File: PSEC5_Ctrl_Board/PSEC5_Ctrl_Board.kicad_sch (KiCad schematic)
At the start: 1 part, among them U1 SM-K26-XCL2GI

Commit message: Beginning Build of Ctrlbd Schematic
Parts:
- removed U1: SM-K26-XCL2GI, SM-K26-XCL2GI:MODULE_SM-K26-XCL2GI, symbol kriak26:SM-K26-XCL2GI
- added J3, J4: ADM6-60-01.5-L-4-2-A-TR, ADM6-60-01.5-L-4-2-A-TR:SAMTEC_ADM6-60-01.5-L-4-2-A-TR, symbol PSEC5_ctrlbd:ADM6-60-01.5-L-4-2-A-TR
- added J5: QSH-040-01-X-D-DP-A, QSH-040-01-X-D-DP-A:SAMTEC_QSH-040-01-X-D-DP-A, symbol PSEC5_ctrlbd:QSH-040-01-X-D-DP-A
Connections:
- new net A01: J3.A01, J4.A01
- new net A02: J3.A02, J4.A02
- new net A05: J3.A05, J4.A05
- new net A06: J3.A06, J4.A06
- new net A09: J3.A09, J4.A09
- new net A10: J3.A10, J4.A10
- new net A13: J3.A13, J4.A13
- new net A16: J3.A16, J4.A16
- new net A19: J3.A19, J4.A19
- new net A22: J3.A22, J4.A22
- new net A25: J3.A25, J4.A25
- new net A28: J3.A28, J4.A28
- new net A31: J3.A31, J4.A31
- new net A34: J3.A34, J4.A34
- new net A37: J3.A37, J4.A37
- new net A40: J3.A40, J4.A40
- new net A43: J3.A43, J4.A43
- new net A45: J3.A45, J4.A45
- new net A49: J3.A49, J4.A49
- new net A53: J3.A53, J4.A53
- new net A57: J3.A57, J4.A57
- new net B03: J3.B03, J4.B03
- new net B04: J3.B04, J4.B04
- new net B07: J3.B07, J4.B07
- new net B08: J3.B08, J4.B08
- new net B11: J3.B11, J4.B11
- new net B14: J3.B14, J4.B14
- new net B17: J3.B17, J4.B17
- new net B20: J3.B20, J4.B20
- new net B23: J3.B23, J4.B23
- new net B26: J3.B26, J4.B26
- new net B29: J3.B29, J4.B29
- new net B32: J3.B32, J4.B32
- new net B35: J3.B35, J4.B35
- new net B38: J3.B38, J4.B38
- new net B41: J3.B41, J4.B41
- new net B43: J3.B43, J4.B43
- new net B47: J3.B47, J4.B47
- new net B51: J3.B51, J4.B51
- new net B55: J3.B55, J4.B55
- new net CLKOUT: J3.A38, J5.23
- new net DISCBIAS: J4.B39, J5.24
- new net GND: J5.G1 (GND_S1), J5.G2 (GND_S1__1), J5.G3 (GND_S1__2), J5.G4 (GND_S1__3)
- new net HBD_power: J3.B59, J3.B60, J4.B59, J4.B60
- new net PICO: J4.B16, J5.33
- new net POCI: J3.A12, J5.03
- new net READBIAS1: J4.B34, J5.18
- new net READBIAS2: J4.B36, J5.20
- new net READCLK: J4.B12, J5.27
- new net READOUT1: J3.A14, J5.05
- new net READOUT2: J3.A15, J5.07
- new net READOUT3: J3.A17, J5.09
- new net READOUT4: J3.A18, J5.11
- new net READOUT5: J3.A20, J5.13
- new net READOUT6: J3.A21, J5.15
- new net READOUT7: J3.A23, J5.17
- new net READOUT8: J3.A24, J5.19
- new net REFCLKOUT: J3.A39, J5.25
- new net RESET: J4.B18, J5.35
- new net SIGNAL1: J4.B40, J5.26
- new net SIGNAL2: J4.B44, J5.28
- new net SIGNAL3: J4.B45, J5.30
- new net SIGNAL4: J4.B46, J5.32
- new net SIGNAL5: J4.B48, J5.34
- new net SIGNAL6: J4.B49, J5.36
- new net SIGNAL7: J5.38
- new net SIGNAL8: J4.B52, J5.40
- new net SIGNAl7: J4.B50
- new net SPICLK: J4.B19, J5.37
- new net THRES1: J4.B22, J5.02
- new net THRES2: J4.B24, J5.04
- new net THRES3: J4.B25, J5.06
- new net THRES4: J4.B27, J5.08
- new net THRES5: J4.B28, J5.10
- new net THRES6: J4.B30, J5.12
- new net THRES7: J4.B31, J5.14
- new net THRES8: J4.B33, J5.16
- new net TRIGGERIN: J4.B13, J5.29
- new net TRIGGEROUT: J3.A26, J5.21
- new net VCOCTRL: J4.B15, J5.31
- new net WBUFBIAS: J4.B37, J5.22
- new net postp_VTUNE: J4.B21, J5.39
- new net prep_VTUNE: J3.A11, J5.01
- new net pwr_1.0_1.8: J3.A44, J3.B42, J4.A44, J4.B42
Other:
- added sheet JTAG (JTAG.kicad_sch)
- note added: "INPUTS"
- note added: "OUTPUTS"

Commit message: A lil more to ctlrbrd, more to come very soon
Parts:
- added J9: QSH-040-01-X-D-DP-A, QSH-040-01-X-D-DP-A:SAMTEC_QSH-040-01-X-D-DP-A, symbol PSEC5_ctrlbd:QSH-040-01-X-D-DP-A
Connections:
- net CLKOUT: no longer J5.23
- net DISCBIAS: now also J5.39; no longer J4.B39, J5.24
- net GND: now also J9.G1 (GND_S1), J9.G2 (GND_S1__1), J9.G3 (GND_S1__2), J9.G4 (GND_S1__3)
- net PICO: now also J9.11; no longer J4.B16, J5.33
- net POCI: now also J9.09; no longer J5.03
- net READBIAS1: now also J5.33; no longer J4.B34, J5.18
- net READBIAS2: now also J5.35; no longer J4.B36, J5.20
- net READOUT1: no longer J5.05
- net READOUT2: no longer J5.07
- net READOUT3: no longer J5.09
- net READOUT4: no longer J5.11
- net READOUT5: no longer J5.13
- net READOUT6: no longer J5.15
- net READOUT7: no longer J5.17
- net READOUT8: no longer J5.19
- net REFCLKOUT: no longer J5.25
- net THRES1: now also J5.01; no longer J4.B22, J5.02
- net THRES2: now also J5.03; no longer J4.B24, J5.04
- net THRES3: now also J5.05; no longer J4.B25, J5.06
- net THRES4: now also J5.07; no longer J4.B27, J5.08
- net THRES5: now also J5.09; no longer J4.B28, J5.10
- net THRES6: now also J5.11; no longer J4.B30, J5.12
- net THRES7: now also J5.13; no longer J4.B31, J5.14
- net THRES8: now also J5.15; no longer J4.B33, J5.16
- net TRIGGEROUT: no longer J5.21
- net WBUFBIAS: now also J5.37; no longer J4.B37, J5.22
- net prep_VTUNE: no longer J5.01
- net READCLK: no longer names the net of J4.B12
- net READCLK: no longer J5.27
- net RESET: no longer names the net of J4.B18
- net RESET: no longer J5.35
- net SIGNAL1: no longer names the net of J4.B40
- net SIGNAL1: no longer J5.26
- net SIGNAL2: no longer names the net of J4.B44
- net SIGNAL2: no longer J5.28
- net SIGNAL3: no longer names the net of J4.B45
- net SIGNAL3: no longer J5.30
- net SIGNAL4: no longer names the net of J4.B46
- net SIGNAL4: no longer J5.32
- net SIGNAL5: no longer names the net of J4.B48
- net SIGNAL5: no longer J5.34
- net SIGNAL6: no longer names the net of J4.B49
- net SIGNAL6: no longer J5.36
- net SIGNAL7 renamed SIGNAL8+
- net SIGNAL8: no longer names the net of J4.B52
- net SIGNAL8: no longer J5.40
- net SIGNAl7: no longer names the net of J4.B50
- net SPICLK: no longer names the net of J4.B19
- net SPICLK: no longer J5.37
- net TRIGGERIN: no longer names the net of J4.B13
- net TRIGGERIN: no longer J5.29
- net VCOCTRL: no longer names the net of J4.B15
- net VCOCTRL: no longer J5.31
- net postp_VTUNE: no longer names the net of J4.B21
- net postp_VTUNE: no longer J5.39
- new net 1V2: J9.02
- new net 1V8: J9.04
- new net 2V5: J9.06
- new net 3V3: J9.08
- new net 5V: J9.10
- new net ADC_SCLK: J9.29
- new net ADC_SDO: J9.33
- new net DAC_SCLK: J9.21
- new net DAC_V_IN: J9.27
- new net OscRefClk: J9.01
- new net Psec5RST: J9.15
- new net Psec5ReadClk: J9.17
- new net Psec5RefClk: J9.03
- new net Psec5TriggerIn: J9.07
- new net Psec5TriggerOut: J9.05
- new net SIGNAL1+: J5.02
- new net SIGNAL1-: J5.04
- new net SIGNAL2+: J5.06
- new net SIGNAL2-: J5.08
- new net SIGNAL3+: J5.10
- new net SIGNAL3-: J5.12
- new net SIGNAL4+: J5.14
- new net SIGNAL4-: J5.16
- new net SIGNAL5+: J5.26
- new net SIGNAL5-: J5.28
- new net SIGNAL6+: J5.30
- new net SIGNAL6-: J5.32
- new net SIGNAL7+: J5.34
- new net SIGNAL7-: J5.36
- new net SIGNAL8-: J5.40
- new net SPIClk: J9.13
- new net SYNC_N: J9.25
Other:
- added sheet SDcard (SDcard.kicad_sch)
- added sheet USB-UART (USBUART.kicad_sch)
- added sheet adcdac (adccad.kicad_sch)
- added sheet ethernet (ethernet.kicad_sch)
- added sheet samtectest (samtectest.kicad_sch)
- sheet Peripherals_Ctrl ports: added ADC_1.8AVDD, ADC_1.8DVDD, ADC_CLK+, ADC_CLK-, ADC_DOUT1+, ADC_DOUT1-, ADC_DOUT2+, ADC_DOUT2-, ADC_DOUT3+, ADC_DOUT3-, ADC_DOUT4+, ADC_DOUT4-, ADC_DOUT5+, ADC_DOUT5-, ADC_DOUT6+, ADC_DOUT6-, ADC_DOUT7+, ADC_DOUT7-, ADC_DOUT8+, ADC_DOUT8-, ADC_VREF, DCO+, DCO-, FCO+, FCO-, READOUT1+, READOUT1-, READOUT2+, READOUT2-, READOUT3+, READOUT3-, READOUT4+, READOUT4-, READOUT5+, READOUT5-, READOUT6+, READOUT6-, READOUT7+, READOUT7-, READOUT8+, READOUT8-; removed none
- note added: "ANALOG SAMTEC"
- note added: "DIGITAL SAMTEC + OTHER"
- note removed: "INPUTS"
- note removed: "OUTPUTS"
- moved on the sheet: J3A, J4A

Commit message: Ports are Finished, wiring and finalization needed
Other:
- sheet JTAG ports: added CLK, RST, TDI, TDO, TMS; removed none
- sheet USB-UART ports: added CTS, RTS, RXD, TXD; removed none
- sheet ethernet ports: added 25MHz, ETH_MDC, ETH_MDIO, ETH_RXD0, ETH_RXD1, ETH_RXD2, ETH_RXD3, ETH_RX_CLK, ETH_RX_CTRL, ETH_TXD0, ETH_TXD1, ETH_TXD2, ETH_TXD3, ETH_TX_CLK, ETH_TX_CTRL, RESETn; removed none

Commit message: Large Updates, Touching up before further aproval
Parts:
- removed J3, J4: ADM6-60-01.5-L-4-2-A-TR, ADM6-60-01.5-L-4-2-A-TR:SAMTEC_ADM6-60-01.5-L-4-2-A-TR, symbol PSEC5_ctrlbd:ADM6-60-01.5-L-4-2-A-TR
- removed J5, J9: QSH-040-01-X-D-DP-A, QSH-040-01-X-D-DP-A:SAMTEC_QSH-040-01-X-D-DP-A, symbol PSEC5_ctrlbd:QSH-040-01-X-D-DP-A
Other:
- removed sheet IO
- removed sheet samtectest
- added sheet DUT_CTRL (DUT_CTRL.kicad_sch)
- added sheet SOM240_1(1.5) (untitled.SOM240_1(1.5).kicad_sch)
- added sheet SOM240_2(1.5) (untitled.SOM240_2(1.5).kicad_sch)
- added sheet power (power.kicad_sch)
- note removed: "ANALOG SAMTEC"
- note removed: "DIGITAL SAMTEC + OTHER"

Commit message: Schematic is "done" ;( (999+ ERC errors)
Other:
- added sheet power2 (power2.kicad_sch)
- sheet JTAG ports: added none; removed CLK, RST, TDI, TDO, TMS
- sheet Peripherals_Ctrl ports: added none; removed ADC_1.8AVDD, ADC_1.8DVDD, ADC_CLK+, ADC_CLK-, ADC_DOUT1+, ADC_DOUT1-, ADC_DOUT2+, ADC_DOUT2-, ADC_DOUT3+, ADC_DOUT3-, ADC_DOUT4+, ADC_DOUT4-, ADC_DOUT5+, ADC_DOUT5-, ADC_DOUT6+, ADC_DOUT6-, ADC_DOUT7+, ADC_DOUT7-, ADC_DOUT8+, ADC_DOUT8-, ADC_VREF, DCO+, DCO-, FCO+, FCO-, READOUT1+, READOUT1-, READOUT2+, READOUT2-, READOUT3+, READOUT3-, READOUT4+, READOUT4-, READOUT5+, READOUT5-, READOUT6+, READOUT6-, READOUT7+, READOUT7-, READOUT8+, READOUT8-
- sheet SDcard ports: added none; removed SD_CLK, SD_CMD, SD_DAT0, SD_DAT1, SD_DAT2, SD_DAT3, SD_DETECT, SD_PWR_EN, SD_SEL
- sheet USB-UART ports: added none; removed CTS, RTS, RXD, TXD
- sheet ethernet ports: added none; removed 25MHz, ETH_MDC, ETH_MDIO, ETH_RXD0, ETH_RXD1, ETH_RXD2, ETH_RXD3, ETH_RX_CLK, ETH_RX_CTRL, ETH_TXD0, ETH_TXD1, ETH_TXD2, ETH_TXD3, ETH_TX_CLK, ETH_TX_CTRL, RESETn

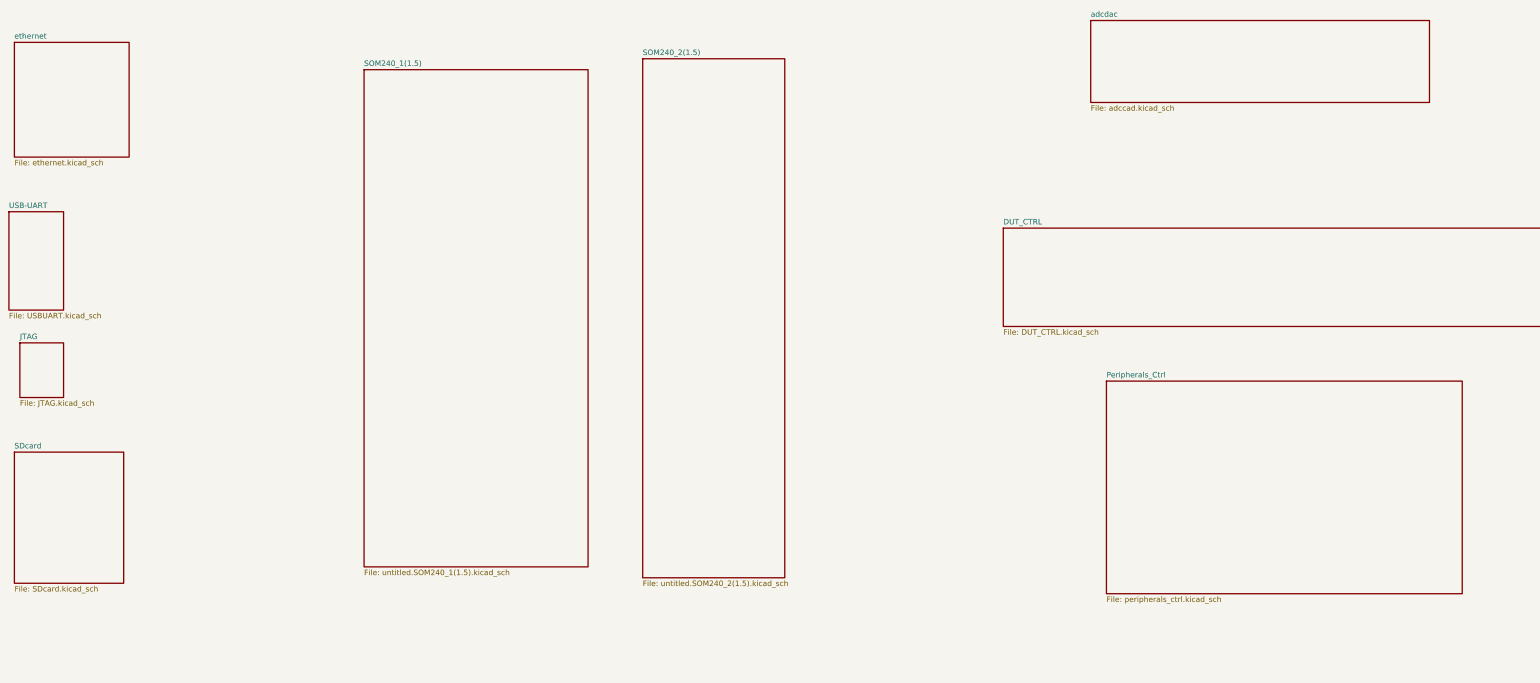
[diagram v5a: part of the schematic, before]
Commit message: Deleted some Pages, still lots of errors :(
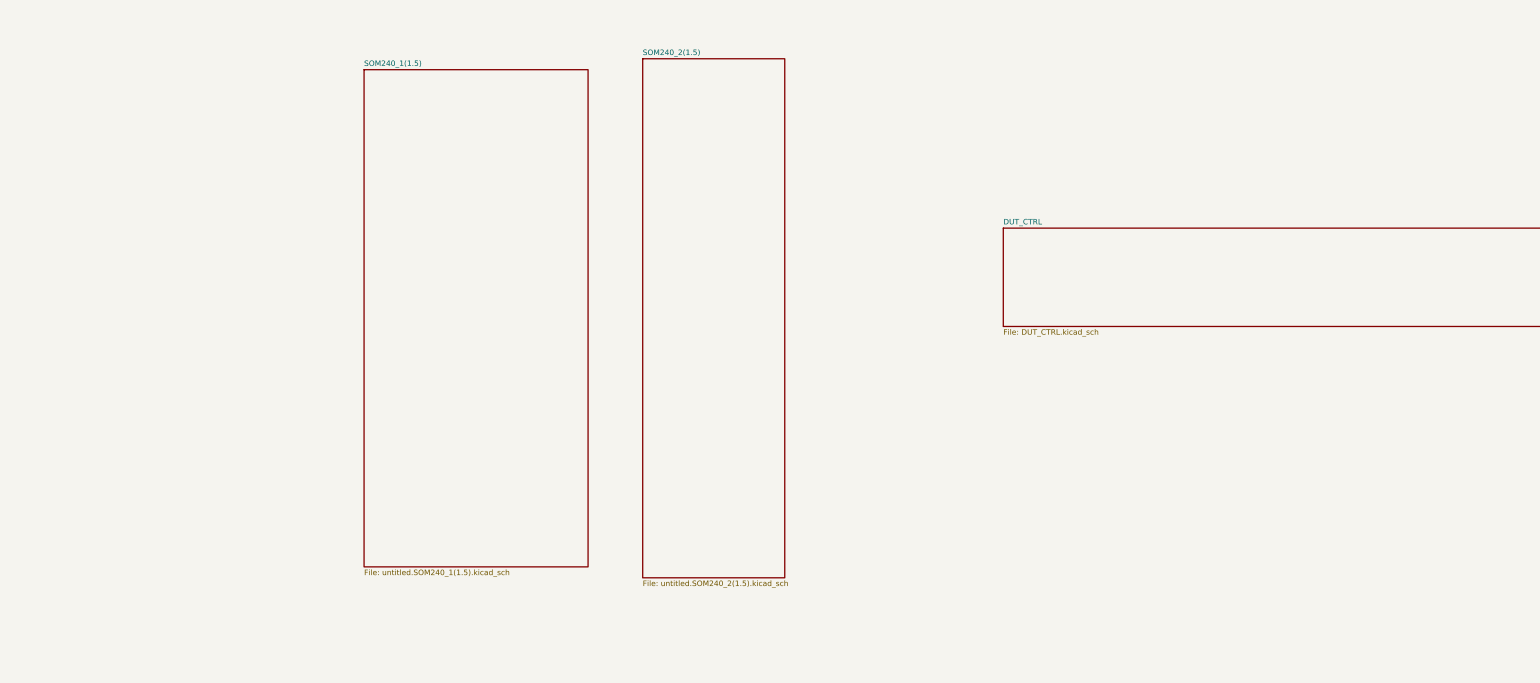
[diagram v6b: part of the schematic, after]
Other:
- removed sheet JTAG
- removed sheet Peripherals_Ctrl
- removed sheet SDcard
- removed sheet USB-UART
- removed sheet adcdac
- removed sheet ethernet
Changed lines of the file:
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@@
-	)
-	(sheet
-		(at 270.35 140.97)
-		(size 82.71 49.42)
-		(fields_autoplaced yes)
-		(stroke
-			(width 0.1524)
-			(type solid)
-		)
-		(fill
-			(color 0 0 0 0.0000)
-		)
-		(property "Sheetname" "Peripherals_Ctrl"
-			(at 270.35 140.2584 0)
-			(effects
-				(font
-					(size 1.27 1.27)
-				)
-				(justify left bottom)
-			)
-		)
-		(property "Sheetfile" "peripherals_ctrl.kicad_sch"
-			(at 270.35 190.9746 0)
-			(effects
-				(font
-					(size 1.27 1.27)
-				)
-				(justify left top)
-			)
-		)
-		(instances
-			(project "PSEC5_Ctrl_Board"
-				(path "/165f2ae6-d522-4adf-a6c4-bb137b209d33"
-					(page "5")
-				)
-			)
-		)
 	)
 	(sheet
@@
 	)
 	(sheet
-		(at 266.7 57.15)
-		(size 78.74 19.05)
-		(fields_autoplaced yes)
-		(stroke
-			(width 0.1524)
-			(type solid)
-		)
-		(fill
-			(color 0 0 0 0.0000)
-		)
-		(property "Sheetname" "adcdac"
-			(at 266.7 56.4384 0)
-			(effects
-				(font
-					(size 1.27 1.27)
-				)
-				(justify left bottom)
-			)
-		)
-		(property "Sheetfile" "adccad.kicad_sch"
-			(at 266.7 76.7846 0)
-			(effects
-				(font
-					(size 1.27 1.27)
-				)
-				(justify left top)
-			)
-		)
-		(instances
-			(project "PSEC5_Ctrl_Board"
-				(path "/165f2ae6-d522-4adf-a6c4-bb137b209d33"
-					(page "6")
-				)
-			)
-		)
-	)
-	(sheet
-		(at 16.51 62.23)
-		(size 26.67 26.67)
-		(fields_autoplaced yes)
-		(stroke
-			(width 0.1524)
-			(type solid)
-		)
-		(fill
-			(color 0 0 0 0.0000)
-		)
-		(property "Sheetname" "ethernet"
-			(at 16.51 61.5184 0)
-			(effects
-				(font
-					(size 1.27 1.27)
-				)
-				(justify left bottom)
-			)
-		)
-		(property "Sheetfile" "ethernet.kicad_sch"
-			(at 16.51 89.4846 0)
-			(effects
-				(font
-					(size 1.27 1.27)
-				)
-				(justify left top)
-			)
-		)
-		(instances
-			(project "PSEC5_Ctrl_Board"
-				(path "/165f2ae6-d522-4adf-a6c4-bb137b209d33"
-					(page "11")
-				)
-			)
-		)
-	)
-	(sheet
-		(at 16.51 157.48)
-		(size 25.4 30.48)
-		(fields_autoplaced yes)
-		(stroke
-			(width 0.1524)
-			(type solid)
-		)
-		(fill
-			(color 0 0 0 0.0000)
-		)
-		(property "Sheetname" "SDcard"
-			(at 16.51 156.7684 0)
-			(effects
-				(font
-					(size 1.27 1.27)
-				)
-				(justify left bottom)
-			)
-		)
-		(property "Sheetfile" "SDcard.kicad_sch"
-			(at 16.51 188.5446 0)
-			(effects
-				(font
-					(size 1.27 1.27)
-				)
-				(justify left top)
-			)
-		)
-		(instances
-			(project "PSEC5_Ctrl_Board"
-				(path "/165f2ae6-d522-4adf-a6c4-bb137b209d33"
-					(page "10")
-				)
-			)
-		)
-	)
-	(sheet
 		(at 49.53 227.33)
 		(size 109.22 43.18)
@@
 				)
 			)
-		)
-	)
-	(sheet
-		(at 15.24 101.6)
-		(size 12.7 22.86)
-		(fields_autoplaced yes)
-		(stroke
-			(width 0.1524)
-			(type solid)
-		)
-		(fill
-			(color 0 0 0 0.0000)
-		)
-		(property "Sheetname" "USB-UART"
-			(at 15.24 100.8884 0)
-			(effects
-				(font
-					(size 1.27 1.27)
-				)
-				(justify left bottom)
-			)
-		)
-		(property "Sheetfile" "USBUART.kicad_sch"
-			(at 15.24 125.0446 0)
-			(effects
-				(font
-					(size 1.27 1.27)
-				)
-				(justify left top)
-			)
-		)
-		(instances
-			(project "PSEC5_Ctrl_Board"
-				(path "/165f2ae6-d522-4adf-a6c4-bb137b209d33"
-					(page "9")
-				)
-			)
-		)
-	)
-	(sheet
-		(at 17.78 132.08)
-		(size 10.16 12.7)
-		(fields_autoplaced yes)
-		(stroke
-			(width 0.1524)
-			(type solid)
-		)
-		(fill
-			(color 0 0 0 0.0000)
-		)
-		(property "Sheetname" "JTAG"
-			(at 17.78 131.3684 0)
-			(effects
-				(font
-					(size 1.27 1.27)
-				)
-				(justify left bottom)
-			)
-		)
-		(property "Sheetfile" "JTAG.kicad_sch"
-			(at 17.78 145.3646 0)
-			(effects
-				(font
-					(size 1.27 1.27)
-				)
-				(justify left top)
-			)
-		)
-		(instances
-			(project "PSEC5_Ctrl_Board"
-				(path "/165f2ae6-d522-4adf-a6c4-bb137b209d33"
-					(page "8")
-				)
-			)

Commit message: ERC "Done" (4 errors left) Schematic "Done"
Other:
- added sheet power_ctrl (power_ctrl.kicad_sch)
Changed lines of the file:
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@@
+	)
+	(sheet
+		(at 35.56 86.36)
+		(size 25.4 50.8)
+		(fields_autoplaced yes)
+		(stroke
+			(width 0.1524)
+			(type solid)
+		)
+		(fill
+			(color 0 0 0 0.0000)
+		)
+		(property "Sheetname" "power_ctrl"
+			(at 35.56 85.6484 0)
+			(effects
+				(font
+					(size 1.27 1.27)
+				)
+				(justify left bottom)
+			)
+		)
+		(property "Sheetfile" "power_ctrl.kicad_sch"
+			(at 35.56 137.7446 0)
+			(effects
+				(font
+					(size 1.27 1.27)
+				)
+				(justify left top)
+			)
+		)
+		(instances
+			(project "PSEC5_Ctrl_Board"
+				(path "/165f2ae6-d522-4adf-a6c4-bb137b209d33"
+					(page "13")
+				)
+			)
+		)
 	)
 	(sheet

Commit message: V2
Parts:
- added H1, H2, H3, H4, H5, H6, H7, H8: MountingHole, MountingHole:MountingHole_3.2mm_M3_DIN965, symbol Mechanical:MountingHole
- added H10, H11, H12, H9: MountingHole, MountingHole:MountingHole_2.2mm_M2_DIN965, symbol Mechanical:MountingHole
